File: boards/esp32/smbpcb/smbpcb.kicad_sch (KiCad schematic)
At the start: 71 parts, among them IC1 MiCS-6814, J1 USB_B_Micro, J2 PMS7003, Q1 SUD08P06-155L, Q2 SS8050_NPN, Q3 SS8050_NPN, SW1 RESET, SW2 RESET, U1 MCP73831-2-OT, U2 TPS61200DRC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

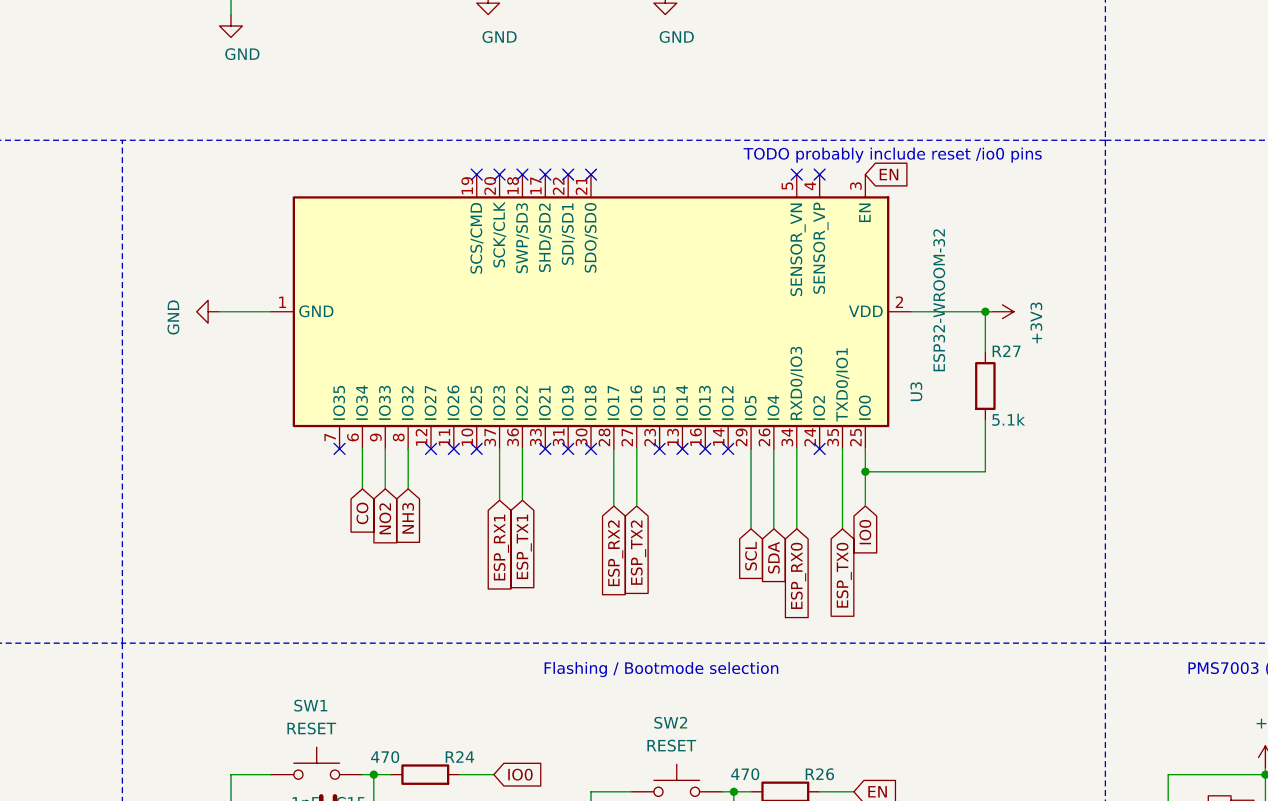
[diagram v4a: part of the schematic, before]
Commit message: added decoupling cap to 3v3 off of esp32 board
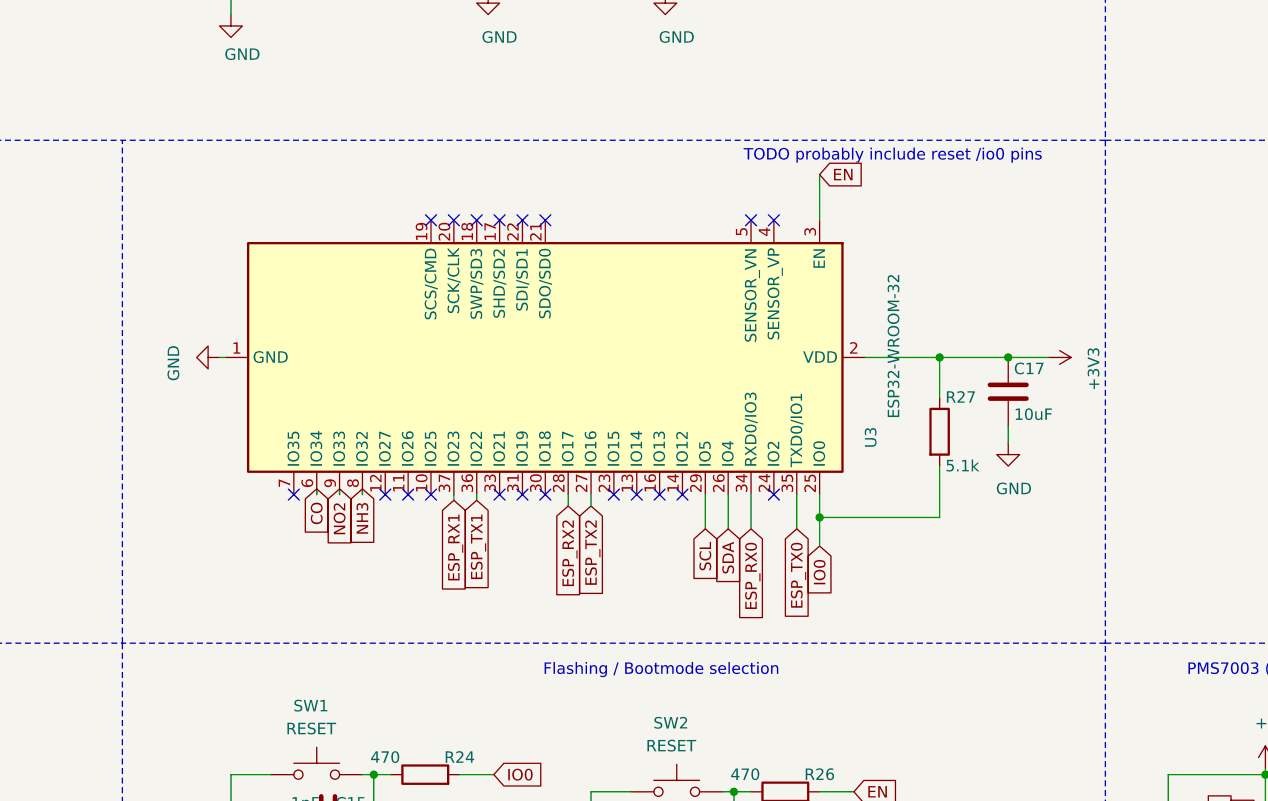
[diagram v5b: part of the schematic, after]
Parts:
- added C17: 10uF, Capacitor_SMD:C_0201_0603Metric, symbol Device:C
- 5V_IN1, EXT_BATT1: mfr_part_num (none) -> C124375
- AUX_CONN1, AUX_CONN2, AUX_CONN3, AUX_CONN4: mfr_part_num (none) -> C124413
- BT1: mfr_part_num (none) -> A2501WR-2P
- C1, C2, C3: mfr_part_num (none) -> UMJ316BC7475KLHTE
- C10, C4, C6, C7, C8: mfr_part_num (none) -> CL21B105KBFNNNE
- C11, C14: mfr_part_num (none) -> CL21A106KAYNNNE
- C12, C13: mfr_part_num (none) -> CC0603KRX7R9BB104
- C15, C16: mfr_part_num (none) -> CL10B102KB8NNNC
- C5: mfr_part_num (none) -> CL21A226MAQNNNE
- C9: mfr_part_num (none) -> CL21C220JBANNNC
- D1, D2, D5: mfr_part_num (none) -> B5819W
- D3, D4: mfr_part_num (none) -> 17-21SURC/S530-A3/TR8
- IC1: Mouser (none) -> 523-MICS-6814; mfr_part_num (none) -> MICS-6814
- J1: mfr_part_num (none) -> MicroXNJ; now in the parts list
- J2: mfr_part_num (none) -> PMS7003
- L1: mfr_part_num (none) -> CMI201209U2R2KT
- Q1: mfr_part_num (none) -> SUD08P06-155L-E3
- Q2, Q3: mfr_part_num (none) -> SS8050
- R1, R15, R25, R6: mfr_part_num (none) -> 0603WAJ0202T5E
- R10: mfr_part_num (none) -> 0603WAJ0821T5E
- R11, R12, R13, R14, R16, R5: mfr_part_num (none) -> 0603WAF1001T5E
- R17, R18: mfr_part_num (none) -> TC0525D4701T5E
- R19: mfr_part_num (none) -> 0603WAF270JT5E
- R2: mfr_part_num (none) -> 0603WAF2004T5E
- R20: mfr_part_num (none) -> 0603WAF1300T5E
- R21: mfr_part_num (none) -> 0603WAF3303T5E
- R22, R23, R4, R7, R8, R9: mfr_part_num (none) -> RMC080510K5%N
- R24, R26, R28: mfr_part_num (none) -> 0603WAF4700T5E
- R27: mfr_part_num (none) -> AECR0805F5K10K9
- R3: mfr_part_num (none) -> 0603WAF1803T5E
- SW1, SW2: mfr_part_num (none) -> ST-1102W-4.3
- U1: mfr_part_num (none) -> MCP73831T-2ACI/OT
- U2: mfr_part_num (none) -> TPS61200DRCR
- U3: mfr_part_num (none) -> ESP32-WROOM-32
- U4: mfr_part_num (none) -> QG-2832TLBFG02
- U5: Mouser (none) -> 262-BME680; mfr_part_num (none) -> BME680
- U6: mfr_part_num (none) -> MH-Z19B
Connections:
- net +3V3: now also C17.1
- net GND: now also C17.2
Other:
- moved on the sheet: R27, U3

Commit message: merging
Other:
- note added: "Breakout Headers"
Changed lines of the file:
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@@
+    (effects (font (size 1.27 1.27)) (justify right bottom))
+  )
+  (text "Breakout Headers\n" (at 71.755 99.06 180)
     (effects (font (size 1.27 1.27)) (justify right bottom))
   )
@@
       (effects (font (size 1.27 1.27)) hide)
     )
-    (property "mfr_part_num" "BME680" (id 4) (at 354.33 55.88 0)
-      (effects (font (size 1.27 1.27)) hide)
-    )
+    (property "mfr_part_num" "BME680" (id 5) (at 354.33 55.88 0)
+      (effects (font (size 1.27 1.27)) hide)
+    )

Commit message: updated bom
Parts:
- C1, C2, C3: Mouser (none) -> 963-UMJ316BC7475KLHT
- C10, C4, C6, C7, C8: Mouser (none) -> 187-CL21B105KBFNNNE
- C11, C14: Mouser (none) -> 187-CL21A106KAYNNNE
- C12, C13: Mouser (none) -> 603-CC603KRX7R9BB104
- C15, C16: Mouser (none) -> 187-CL10B102KB8NNNC
- C17: Mouser (none) -> 187-CL10A106KP8NNNC
- C5: Mouser (none) -> 187-CL21A226MAQNNNE
- C9: Mouser (none) -> 187-CL21C220JBANNNC
- D1, D2, D5: Mouser (none) -> 833-B5819W-TP
- D3, D4: Mouser (none) -> 755-SML-H12U8TT86C
- L1: Mouser (none) -> 652-CVH201205-2R2M
- Q1: Mouser (none) -> 781-SUD08P06-155L-E3
- Q2, Q3: Mouser (none) -> 750-SS8050-G
- R1, R15, R25, R6: Mouser (none) -> 71-TNPU06032K00AWEN
- R10: Mouser (none) -> 667-ERJ-UP3J821V
- R11, R12, R13, R14, R16, R5: Mouser (none) -> 71-TNPU06031K00AWEN
- R17, R18: Mouser (none) -> 667-ERJ-UP3D4701V
- R19: Mouser (none) -> 652-CMP0603AFX-27R0L
- R2: Mouser (none) -> 667-ERJ-U03F2204V
- R20: Mouser (none) -> 667-ERJ-UP3F1300V
- R21: Mouser (none) -> 667-ERJ-3RED3303V
- R22, R23, R4, R7, R8, R9: Mouser (none) -> 71-TNPU080510K0AWEN
- R24, R26, R28: Mouser (none) -> 667-ERJ-UP3J471V
- R27: Mouser (none) -> 71-CRCW06035K10FKEAC
- R3: Mouser (none) -> 71-CRCW0603180KFKEAC
- U1: Mouser (none) -> 579-MCP73831T-2ACIOT
- U2: Mouser (none) -> 595-TPS61200DRCR
- U3: Mouser (none) -> 356-ESPWROOM3216MB

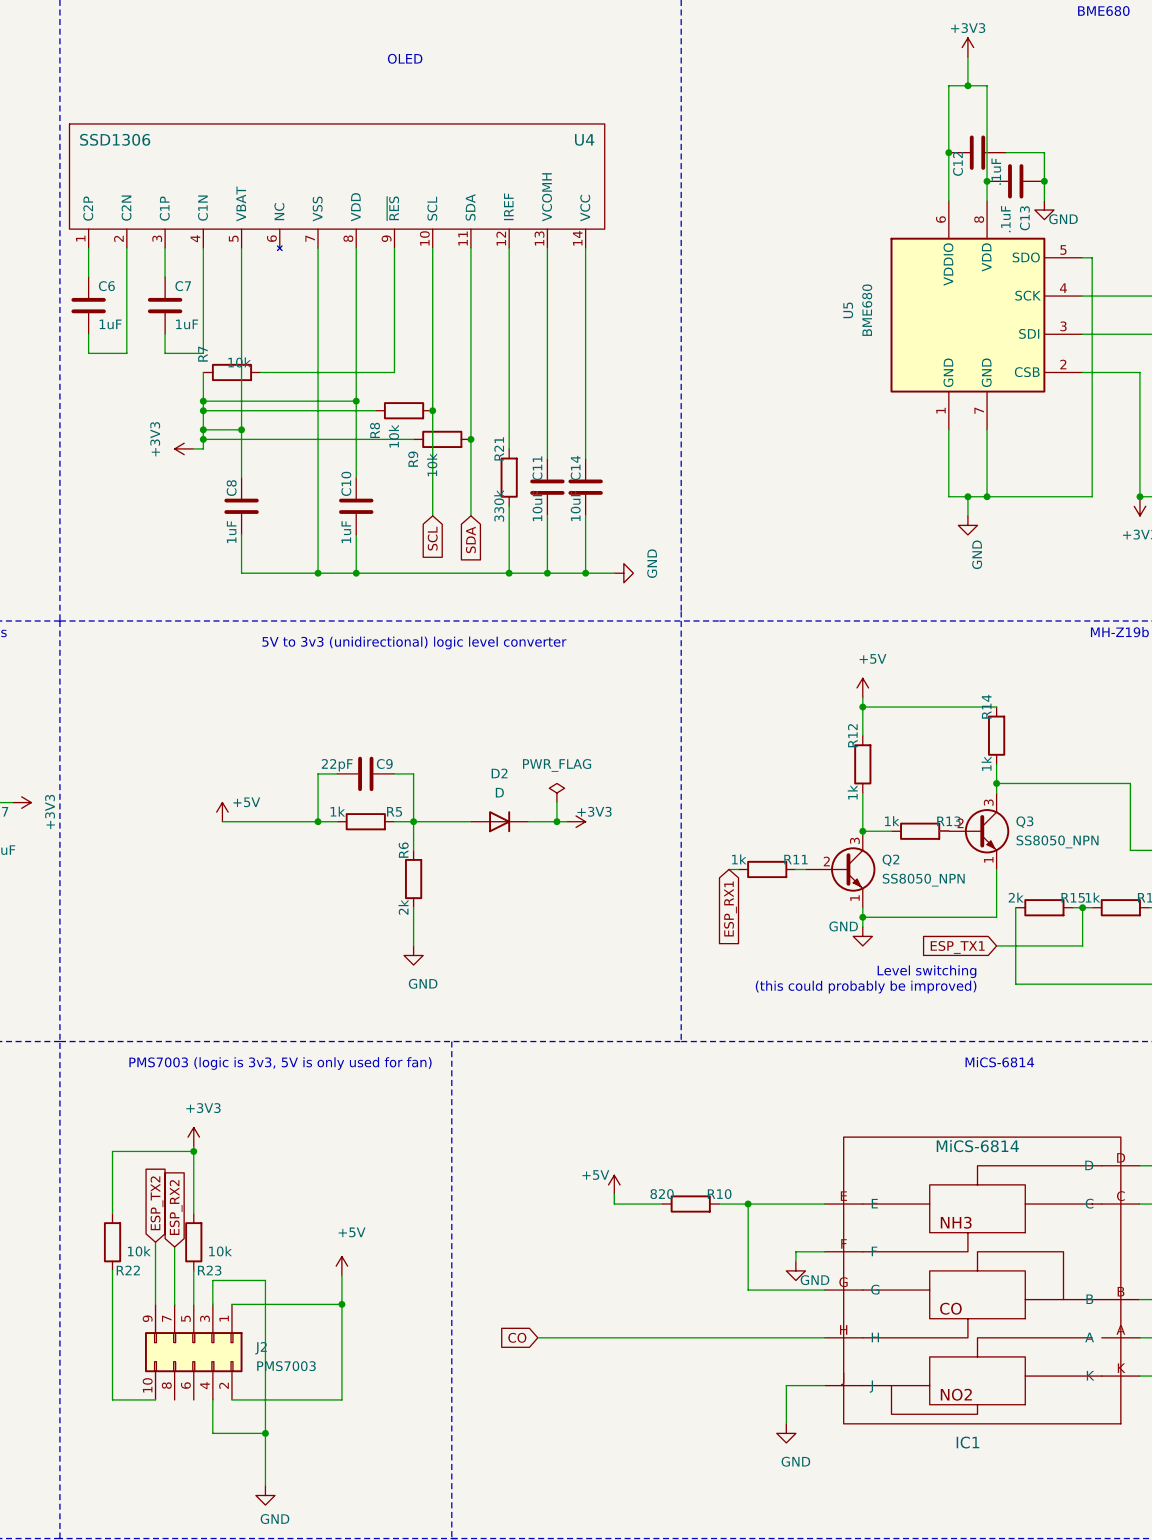
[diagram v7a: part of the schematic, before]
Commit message: made everything 0805 or bigger except that nagging BGA Linear regulator and the bme680
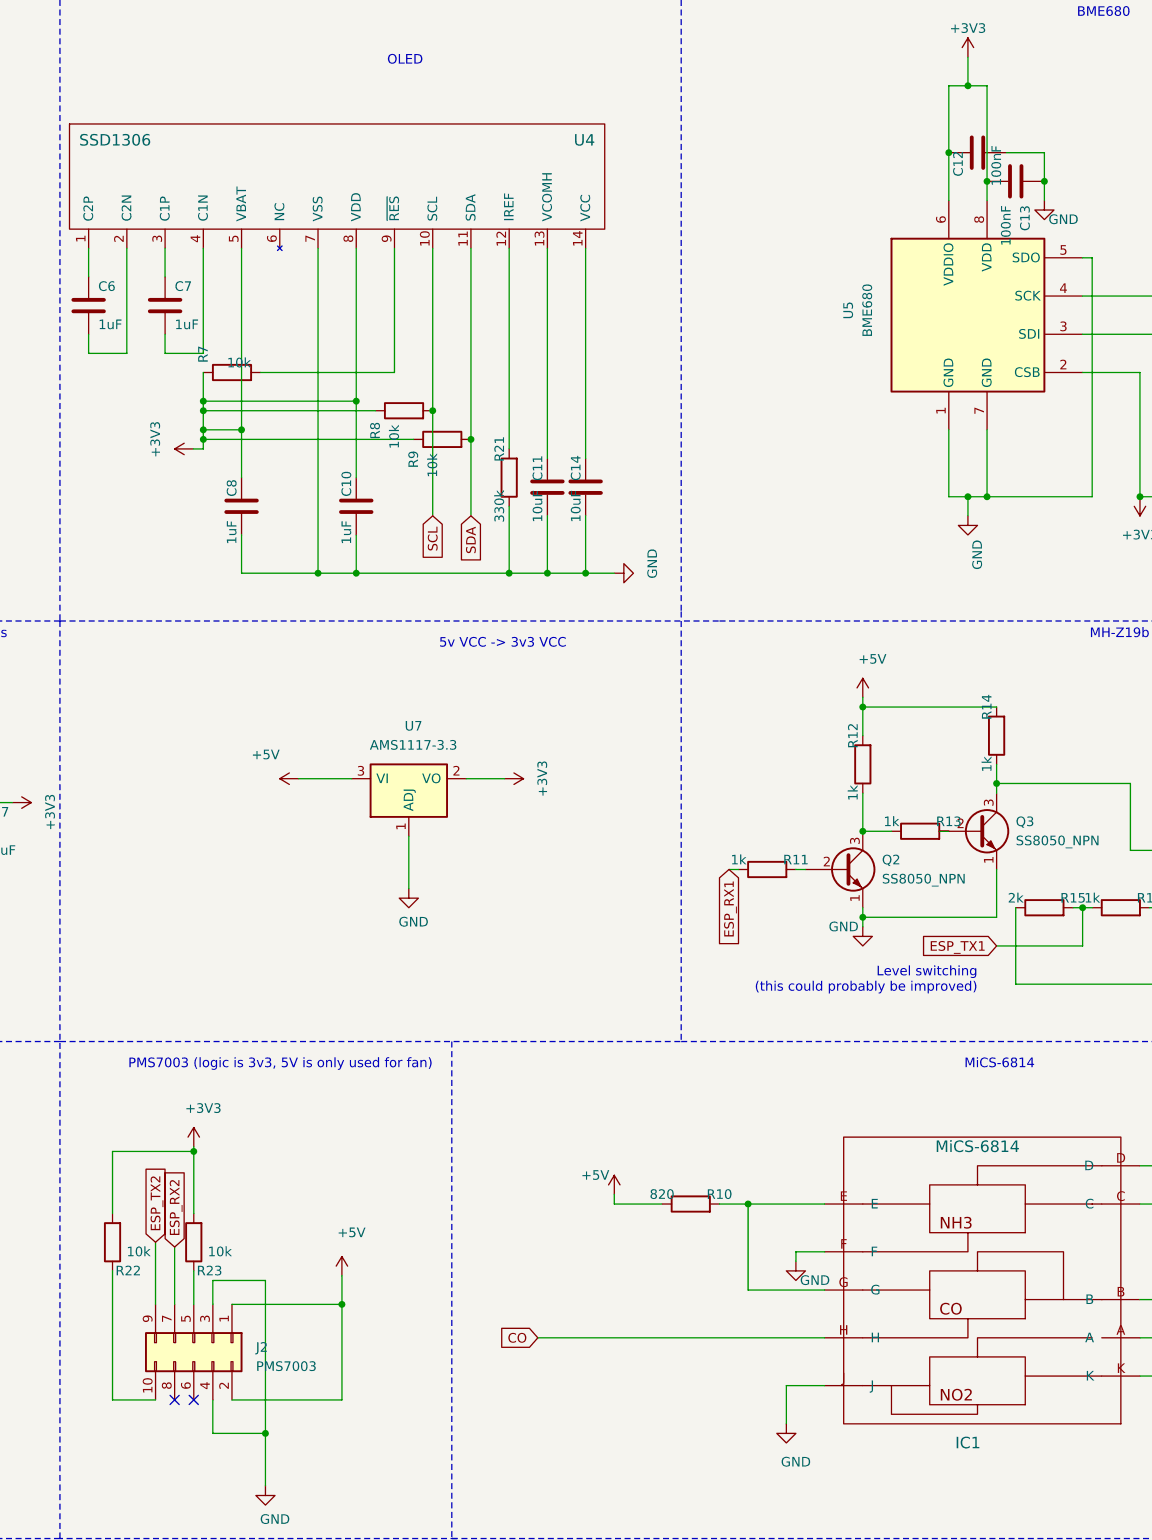
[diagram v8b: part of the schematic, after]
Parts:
- removed C9: 22pF, Capacitor_SMD:C_0805_2012Metric, symbol Device:C
- removed D2: D, Diode_SMD:D_SOD-123, symbol Device:D
- removed R5: 1k, Capacitor_SMD:C_0201_0603Metric, symbol Device:R
- removed R6: 2k, Capacitor_SMD:C_0201_0603Metric, symbol Device:R
- added U7: AMS1117-3.3, Package_TO_SOT_SMD:SOT-223-3_TabPin2, symbol Regulator_Linear:AMS1117
- 5V_IN1, EXT_BATT1: footprint Connector_PinHeader_1.00mm:PinHeader_1x02_P1.00mm_Vertical -> Connector_PinHeader_2.54mm:PinHeader_1x02_P2.54mm_Vertical
- AUX_CONN1, AUX_CONN2, AUX_CONN3, AUX_CONN4: footprint Connector_PinHeader_1.00mm:PinHeader_1x04_P1.00mm_Vertical -> Connector_PinHeader_2.54mm:PinHeader_1x04_P2.54mm_Vertical
- C1, C2, C3: mfr_part_num UMJ316BC7475KLHTE -> (none)
- C10, C4, C6, C7, C8: mfr_part_num CL21B105KBFNNNE -> (none)
- C11, C14: LCSC C15850 -> C40894; Mouser 187-CL21A106KAYNNNE -> 0805X106K250NT; mfr_part_num CL21A106KAYNNNE -> (none)
- C12, C13: value .1uF -> 100nF; footprint Capacitor_SMD:C_0201_0603Metric -> Capacitor_SMD:C_0805_2012Metric; LCSC C14663 -> C49678; Mouser 603-CC603KRX7R9BB104 -> CC0805KRX7R9BB104; mfr_part_num CC0603KRX7R9BB104 -> (none)
- C15, C16: footprint Capacitor_SMD:C_0201_0603Metric -> Capacitor_SMD:C_0805_2012Metric; LCSC C1588 -> C309046; Mouser 187-CL10B102KB8NNNC -> TCC0805X7R102K501DTS; mfr_part_num CL10B102KB8NNNC -> (none)
- C17: footprint Capacitor_SMD:C_0201_0603Metric -> Capacitor_SMD:C_0805_2012Metric; LCSC C19702 -> C40894; Mouser 187-CL10A106KP8NNNC -> 0805X106K250NT; mfr_part_num CL10A106KP8NNNC -> (none)
- C5: mfr_part_num CL21A226MAQNNNE -> (none)
- D1, D5: mfr_part_num B5819W -> (none)
- D3, D4: mfr_part_num 17-21SURC/S530-A3/TR8 -> (none)
- L1: mfr_part_num CMI201209U2R2KT -> (none)
- Q1: mfr_part_num SUD08P06-155L-E3 -> (none)
- Q2, Q3: mfr_part_num SS8050 -> (none)
- R1, R15, R25: footprint Capacitor_SMD:C_0201_0603Metric -> Capacitor_SMD:C_0805_2012Metric; LCSC C25590 -> C328391; Mouser 71-TNPU06032K00AWEN -> AECR0805F2K00K9; mfr_part_num 0603WAJ0202T5E -> (none)
- R10: footprint Capacitor_SMD:C_0201_0603Metric -> Capacitor_SMD:C_0805_2012Metric; LCSC C25259 -> C352174; Mouser 667-ERJ-UP3J821V -> AECR0805F820RK9; mfr_part_num 0603WAJ0821T5E -> (none)
- R11, R12, R13, R14, R16: footprint Capacitor_SMD:C_0201_0603Metric -> Capacitor_SMD:C_0805_2012Metric; LCSC C21190 -> C416075; Mouser 71-TNPU06031K00AWEN -> CR-05FL7----1K; mfr_part_num 0603WAF1001T5E -> (none)
- R17, R18: LCSC C64354 -> C844941; Mouser 667-ERJ-UP3D4701V -> CRCW08054K70FKEA; mfr_part_num TC0525D4701T5E -> (none)
- R19: footprint Capacitor_SMD:C_0201_0603Metric -> Capacitor_SMD:C_0805_2012Metric; LCSC C25190 -> C104178; Mouser 652-CMP0603AFX-27R0L -> RTT0527R0FTP; mfr_part_num 0603WAF270JT5E -> (none)
- R2: footprint Capacitor_SMD:C_0201_0603Metric -> Capacitor_SMD:C_0805_2012Metric; LCSC C22976 -> C325853; Mouser 667-ERJ-U03F2204V -> RMC08052M5%N; mfr_part_num 0603WAF2004T5E -> (none)
- R20: footprint Capacitor_SMD:C_0201_0603Metric -> Capacitor_SMD:C_0805_2012Metric; LCSC C22796 -> C17451; Mouser 667-ERJ-UP3F1300V -> CR0805-FX-1300ELF; mfr_part_num 0603WAF1300T5E -> (none)
- R21: footprint Capacitor_SMD:C_0201_0603Metric -> Capacitor_SMD:C_0805_2012Metric; LCSC C23137 -> C328392; Mouser 667-ERJ-3RED3303V -> AECR0805F330KK9; mfr_part_num 0603WAF3303T5E -> (none)
- R22, R23, R4, R7, R8, R9: mfr_part_num RMC080510K5%N -> (none)
- R24, R26, R28: footprint Capacitor_SMD:C_0201_0603Metric -> Capacitor_SMD:C_0805_2012Metric; LCSC C23179 -> C136570; Mouser 667-ERJ-UP3J471V -> (none); mfr_part_num 0603WAF4700T5E -> (none)
- R27: mfr_part_num AECR0805F5K10K9 -> (none)
- R3: footprint Capacitor_SMD:C_0201_0603Metric -> Capacitor_SMD:C_0805_2012Metric; LCSC C22827 -> C352261; Mouser 71-CRCW0603180KFKEAC -> AECR0805F180KK9; mfr_part_num 0603WAF1803T5E -> (none)
- U1: mfr_part_num MCP73831T-2ACI/OT -> (none)
- U2: mfr_part_num TPS61200DRCR -> (none)
- U3: mfr_part_num ESP32-WROOM-32 -> (none)
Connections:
- net +3V3: now also U7.2 (VO)
- net +5V: now also U7.3 (VI)
- net GND: now also U7.1 (ADJ)
- no-connect marks 25 -> 27
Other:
- note added: "5v VCC -> 3v3 VCC"
- note removed: "5V to 3v3 (unidirectional) logic level converter"
